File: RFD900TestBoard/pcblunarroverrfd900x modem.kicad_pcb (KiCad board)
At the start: 2 copper layers, 5.9 x 6.4 mm, 4 parts, among them J1 Barrel_Jack, J2 Conn_02x08_Counter_Clockwise, U1 ESP32-DEVKIT-V1, U2 GPS-15136

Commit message: edits
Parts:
- added R1: R, Resistor_THT:R_Axial_DIN0204_L3.6mm_D1.6mm_P1.90mm_Vertical, F.Cu at (142.8, 68.8)
- added R2: R, Resistor_THT:R_Axial_DIN0204_L3.6mm_D1.6mm_P1.90mm_Vertical, F.Cu at (177.9, 120.7)
- added R3: R, Resistor_THT:R_Axial_DIN0204_L3.6mm_D1.6mm_P1.90mm_Vertical, F.Cu at (177.9, 123.8)
- added R4: R, Resistor_THT:R_Axial_DIN0204_L3.6mm_D1.6mm_P1.90mm_Vertical, F.Cu at (177.9, 127.0)
- moved J1 63.7 mm to (206.6, 132.1), turned to 0 degrees
- moved U2 34.6 mm to (156.3, 107.1)
- moved U1 25.3 mm to (117.4, 90.7)
- moved J2 19.2 mm to (127.6, 55.9), turned to 0 degrees
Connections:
- U1 pad 11: unconnected-(U1-D21-Pad11) -> /SDA
- U1 pad 14: /CTS -> /SCL
- U1 pad 27: unconnected-(U1-D12-Pad27) -> /CTS
- U2 pad J7_1: unconnected-(U2D-SCL/SCK_J7-PadJ7_1) -> /SCL
- U2 pad J7_4: unconnected-(U2D-SDA/~{CS}_J7-PadJ7_4) -> /SDA
- U2 pad J7_7: unconnected-(U2D-3.3V_J7-PadJ7_7) -> +3.3V
- U2 pad J7_9: unconnected-(U2D-GND_J7-PadJ7_9) -> GND
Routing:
- net GND: track 137.0 -> 0.00 mm
- net +5V: track 82.1 -> 0.00 mm

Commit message: edits
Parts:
- removed R1, R2, R3, R4: R, Resistor_THT:R_Axial_DIN0204_L3.6mm_D1.6mm_P1.90mm_Vertical
- added 0.1uF1: C_Polarized_US, Capacitor_THT:CP_Radial_D5.0mm_P2.00mm, F.Cu at (169.3, 110.2)
- added 0.1uF3: C_Polarized_US, Capacitor_THT:CP_Radial_D5.0mm_P2.00mm, F.Cu at (136.7, 61.4)
- added 0.1uf2: C_Polarized_US, Capacitor_THT:CP_Radial_D5.0mm_P2.00mm, F.Cu at (104.0, 45.9)
- added 1000uf1: C_Polarized_US, Capacitor_THT:CP_Radial_D5.0mm_P2.00mm, F.Cu at (117.6, 49.4)
- added 10uF1: C_Polarized_US, Capacitor_THT:CP_Radial_D5.0mm_P2.00mm, F.Cu at (169.1, 99.8)
- added 10uF2: C_Polarized_US, Capacitor_THT:CP_Radial_D5.0mm_P2.00mm, F.Cu at (137.8, 67.0)
- added D1: LED, LED_THT:LED_D3.0mm, F.Cu at (46.0, 144.5)
- added J10: Conn_02x01, Connector_PinHeader_2.54mm:PinHeader_2x01_P2.54mm_Vertical, F.Cu at (109.8, 160.9)
- added J11: Conn_02x01, Connector_PinHeader_2.54mm:PinHeader_2x01_P2.54mm_Vertical, F.Cu at (109.8, 165.5)
- added J12: Conn_02x01, Connector_PinHeader_2.54mm:PinHeader_2x01_P2.54mm_Vertical, F.Cu at (109.8, 170.1)
- added J13: Conn_02x01, Connector_PinHeader_2.54mm:PinHeader_2x01_P2.54mm_Vertical, F.Cu at (116.9, 151.8)
- added J14: Conn_02x01, Connector_PinHeader_2.54mm:PinHeader_2x01_P2.54mm_Vertical, F.Cu at (116.9, 156.4)
- added J16: Conn_02x01, Connector_PinHeader_2.54mm:PinHeader_2x01_P2.54mm_Vertical, F.Cu at (164.2, 102.1)
- added J17: Conn_02x01, Connector_PinHeader_2.54mm:PinHeader_2x01_P2.54mm_Vertical, F.Cu at (160.4, 102.1)
- added J18: Conn_01x11, Connector_PinHeader_2.54mm:PinHeader_1x11_P2.54mm_Vertical, F.Cu at (81.8, 58.2)
- added J3: Conn_02x01, Connector_PinHeader_2.54mm:PinHeader_2x01_P2.54mm_Vertical, F.Cu at (102.6, 151.8)
- added J4: Conn_02x01, Connector_PinHeader_2.54mm:PinHeader_2x01_P2.54mm_Vertical, F.Cu at (102.6, 156.4)
- added J5: Conn_02x01, Connector_PinHeader_2.54mm:PinHeader_2x01_P2.54mm_Vertical, F.Cu at (102.6, 160.9)
- added J6: Conn_02x01, Connector_PinHeader_2.54mm:PinHeader_2x01_P2.54mm_Vertical, F.Cu at (102.6, 165.5)
- added J7: Conn_02x01, Connector_PinHeader_2.54mm:PinHeader_2x01_P2.54mm_Vertical, F.Cu at (102.6, 170.1)
- added J8: Conn_02x01, Connector_PinHeader_2.54mm:PinHeader_2x01_P2.54mm_Vertical, F.Cu at (109.8, 151.8)
- added J9: Conn_02x01, Connector_PinHeader_2.54mm:PinHeader_2x01_P2.54mm_Vertical, F.Cu at (109.8, 156.4)
- J2: footprint Connector_DIN:DIN41612_B2_2x8_Male_Horizontal_THT -> Connector_PinHeader_2.54mm:PinHeader_2x08_P2.54mm_Vertical
- moved J1 104.8 mm to (156.6, 40.0), turned to 180 degrees
- moved U2 65.1 mm to (185.3, 48.8), turned to 180 degrees
- moved J2 19.7 mm to (116.2, 39.8), turned to 90 degrees
- moved U1 8.48 mm to (118.5, 82.3)
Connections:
- U1 pad 1: +3.3V -> unconnected-(U1-3V3-Pad1)
- U1 pad 10: unconnected-(U1-D19-Pad10) -> INT
- U1 pad 11: /SDA -> SDA
- U1 pad 12: /TX -> TX-esp
- U1 pad 13: /RX -> RX-esp
- U1 pad 14: /SCL -> SCL
- U1 pad 15: /RTS -> RTS-esp
- U1 pad 23: unconnected-(U1-D25-Pad23) -> CTS-esp
- U1 pad 27: /CTS -> unconnected-(U1-D12-Pad27)
- U1 pad 4: /RESET -> unconnected-(U1-D2-Pad4)
- U1 pad 5: /SAFE -> unconnected-(U1-D4-Pad5)
- U1 pad 6: /TX2 -> TX-jet
- U1 pad 7: /RX2 -> RX-jet
- U1 pad 8: /INT -> unconnected-(U1-D5-Pad8)
- U1 pad 9: unconnected-(U1-D18-Pad9) -> RST
- U2 pad J1_2: /TX2 -> unconnected-(U2A-TX2_J1-PadJ1_2)
- U2 pad J1_3: /RX2 -> unconnected-(U2A-RX2_J1-PadJ1_3)
- U2 pad J1_4: +3.3V -> unconnected-(U2A-3.3V_J1-PadJ1_4)
- U2 pad J6_2: unconnected-(U2C-RTK_STAT-PadJ6_2) -> RTK-jet
- U2 pad J6_4: /RESET -> RST
- U2 pad J6_5: /SAFE -> unconnected-(U2C-~{SAFE}-PadJ6_5)
- U2 pad J6_6: /INT -> INT
- U2 pad J7_1: /SCL -> Net-(J12-Pin_1)
- U2 pad J7_4: /SDA -> Net-(J11-Pin_1)
- U2 pad J7_5: unconnected-(U2D-RX2_J7-PadJ7_5) -> Net-(J17-Pin_2)
- U2 pad J7_6: unconnected-(U2D-TX2_J7-PadJ7_6) -> Net-(J16-Pin_2)
- U2 pad J7_7: +3.3V -> unconnected-(U2D-3.3V_J7-PadJ7_7)
- U2 pad J7_8: unconnected-(U2D-5V_J7-PadJ7_8) -> +5V
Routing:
- net +5V: track 0.00 -> 127.6 mm
- net GND: track 0.00 -> 75.9 mm
- net TX2-jet: track 0.00 -> 17.1 mm
- net Net-(J17-Pin_2): track 0.00 -> 9.19 mm
- net Net-(J16-Pin_2): track 0.00 -> 9.07 mm
- net RX2-jet: track 0.00 -> 2.72 mm
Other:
- outline, holes or cut-outs redrawn

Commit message: changes
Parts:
- moved J10 122.7 mm to (101.5, 38.5), turned to 180 degrees
- moved J7 120.2 mm to (101.8, 50.0), turned to 180 degrees
- moved J6 120.0 mm to (135.9, 50.3), turned to 90 degrees
- moved J5 114.5 mm to (132.3, 50.3), turned to 90 degrees
- moved J9 114.5 mm to (101.8, 42.1), turned to 180 degrees
- moved J4 109.1 mm to (128.5, 50.4), turned to 90 degrees
- moved J8 106.0 mm to (101.8, 46.0), turned to 180 degrees
- moved J3 103.8 mm to (124.8, 50.4), turned to 90 degrees
- moved D1 103.0 mm to (99.5, 56.5), turned to 180 degrees
- moved J12 78.2 mm to (142.3, 99.0), turned to 180 degrees
- moved J11 68.3 mm to (142.2, 105.4), turned to 180 degrees
- moved J14 67.0 mm to (156.3, 102.1), turned to 90 degrees
- moved J13 60.9 mm to (152.2, 102.1), turned to 90 degrees
- moved 0.1uf2 47.4 mm to (150.9, 38.9), turned to -90 degrees
- moved 1000uf1 28.6 mm to (143.9, 38.2), turned to -90 degrees
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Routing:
- net RX2-jet: track 2.72 -> 140.1 mm
- net TX2-jet: track 17.1 -> 127.8 mm
- net SCL-jet: track 0.00 -> 103.1 mm
- net SDA-jet: track 0.00 -> 94.4 mm
- net INT: track 0.00 -> 92.3 mm, vias 0 -> 6
- net SDA: track 0.00 -> 88.4 mm
- net RX-esp: track 0.00 -> 80.6 mm
- net RTK-jet: track 0.00 -> 78.7 mm
- net RST: track 0.00 -> 69.1 mm, vias 0 -> 2
- net RTS-esp: track 0.00 -> 63.2 mm, vias 0 -> 2
- net TX-jet: track 0.00 -> 58.7 mm
- net TX-esp: track 0.00 -> 53.9 mm, vias 0 -> 1
- net SCL: track 0.00 -> 50.5 mm
- net RX-jet: track 0.00 -> 50.4 mm, vias 0 -> 1
- net Net-(J10-Pin_1): track 0.00 -> 41.5 mm
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- added copper zone on B.Cu, net GND

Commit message: hi
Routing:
- net GND: track 83.8 -> 68.1 mm
- net +5V: track 146.9 -> 131.8 mm
- net INT: track 92.3 -> 88.2 mm, vias 6 -> 5
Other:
- copper layers 2 -> 4
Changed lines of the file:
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@@
 	(layers
 		(0 "F.Cu" signal)
+		(4 "In1.Cu" signal)
+		(6 "In2.Cu" signal)
 		(2 "B.Cu" signal)
 		(9 "F.Adhes" user "F.Adhesive")
@@
 	)
 	(setup
+		(stackup
+			(layer "F.SilkS"
+				(type "Top Silk Screen")
+			)
+			(layer "F.Paste"
+				(type "Top Solder Paste")
+			)
+			(layer "F.Mask"
+				(type "Top Solder Mask")
+				(thickness 0.01)
+			)
+			(layer "F.Cu"
+				(type "copper")
+				(thickness 0.035)
+			)
+			(layer "dielectric 1"
+				(type "prepreg")
+				(thickness 0.1)
+				(material "FR4")
+				(epsilon_r 4.5)
+				(loss_tangent 0.02)
+			)
+			(layer "In1.Cu"
+				(type "copper")
+				(thickness 0.035)
+			)
+			(layer "dielectric 2"
+				(type "core")
+				(thickness 1.24)
+				(material "FR4")
+				(epsilon_r 4.5)
+				(loss_tangent 0.02)
+			)
+			(layer "In2.Cu"
+				(type "copper")
+				(thickness 0.035)
+			)
+			(layer "dielectric 3"
+				(type "prepreg")
+				(thickness 0.1)
+				(material "FR4")
+				(epsilon_r 4.5)
+				(loss_tangent 0.02)
+			)
+			(layer "B.Cu"
+				(type "copper")
+				(thickness 0.035)
+			)
+			(layer "B.Mask"
+				(type "Bottom Solder Mask")
+				(thickness 0.01)
+			)
+			(layer "B.Paste"
+				(type "Bottom Solder Paste")
+			)
+			(layer "B.SilkS"
+				(type "Bottom Silk Screen")
+			)
+			(copper_finish "None")
+			(dielectric_constraints no)
+		)
 		(pad_to_mask_clearance 0)
 		(allow_soldermask_bridges_in_footprints no)
@@
 	)
 	(segment
-		(start 171.674888 96.475112)
-		(end 171.674888 106.730224)
-		(width 0.7)
-		(layer "F.Cu")
-		(net 1)
-	)
-	(segment
 		(start 137.46 69.34)
 		(end 137.8 69)
@@
 	)
 	(segment
-		(start 171.32 90.72)
-		(end 171.32 96.120224)
-		(width 0.7)
-		(layer "F.Cu")
-		(net 1)
-	)
-	(segment
 		(start 165.410058 39.95)
 		(end 175.011058 49.551)
@@
 	)
 	(segment
-		(start 169.674888 96.475112)
-		(end 169.674888 91.614888)
-		(width 0.7)
-		(layer "F.Cu")
-		(net 2)
-	)
-	(segment
 		(start 123.69 33.44)
 		(end 123.55 33.3)
@@
 	)
 	(segment
-		(start 169.919776 106.975112)
-		(end 169.919776 96.72)
-		(width 0.7)
-		(layer "F.Cu")
-		(net 2)
-	)
-	(segment
 		(start 143.95 38.25)
 		(end 143.95 35.95)
@@
 	)
 	(via
-		(at 121.25 68.25)
-		(size 0.6)
-		(drill 0.3)
-		(layers "F.Cu" "B.Cu")
-		(net 48)
-	)
-	(via
 		(at 123.5 71.45)
 		(size 0.6)
@@
 	)
 	(segment
-		(start 121.3 68.25)
-		(end 121.25 68.25)
-		(width 0.2)
-		(layer "B.Cu")
-		(net 48)
-	)
-	(segment
 		(start 151.85 54.35)
 		(end 151.85 64.2)
@@
 	)
 	(segment
-		(start 103.67 87.12)
-		(end 121.3 69.49)
-		(width 0.2)
-		(layer "B.Cu")
-		(net 48)
-	)
-	(segment
 		(start 140.95 57.15)
 		(end 135.2 57.15)
@@
 	)
 	(segment
-		(start 141.1 57)
-		(end 140.95 57.15)
+		(start 109.1 85.85)
+		(end 104.94 85.85)
 		(width 0.2)
 		(layer "B.Cu")
@@
 	(segment
 		(start 123.5 71.45)
-		(end 121.25 69.2)
+		(end 109.1 85.85)
+		(width 0.2)
+		(layer "B.Cu")
+		(net 48)
+	)
+	(segment
+		(start 141.1 57)
+		(end 140.95 57.15)
 		(width 0.2)
 		(layer "B.Cu")
@@
 	)
 	(segment
-		(start 121.25 68.25)
-		(end 121.2 68.25)
-		(width 0.2)
-		(layer "B.Cu")
-		(net 48)
-	)
-	(segment
 		(start 135.2 57.15)
 		(end 135.2 59.3)
@@
 	)
 	(segment
-		(start 121.3 69.49)
-		(end 121.3 68.25)
-		(width 0.2)
-		(layer "B.Cu")
-		(net 48)
-	)
-	(segment
-		(start 121.25 69.2)
-		(end 121.25 68.25)
+		(start 104.94 85.85)
+		(end 103.67 87.12)
 		(width 0.2)
 		(layer "B.Cu")
@@
 		(min_thickness 0.25)
 		(filled_areas_thickness no)
-		(fill
+		(fill yes
 			(thermal_gap 0.5)
 			(thermal_bridge_width 0.5)

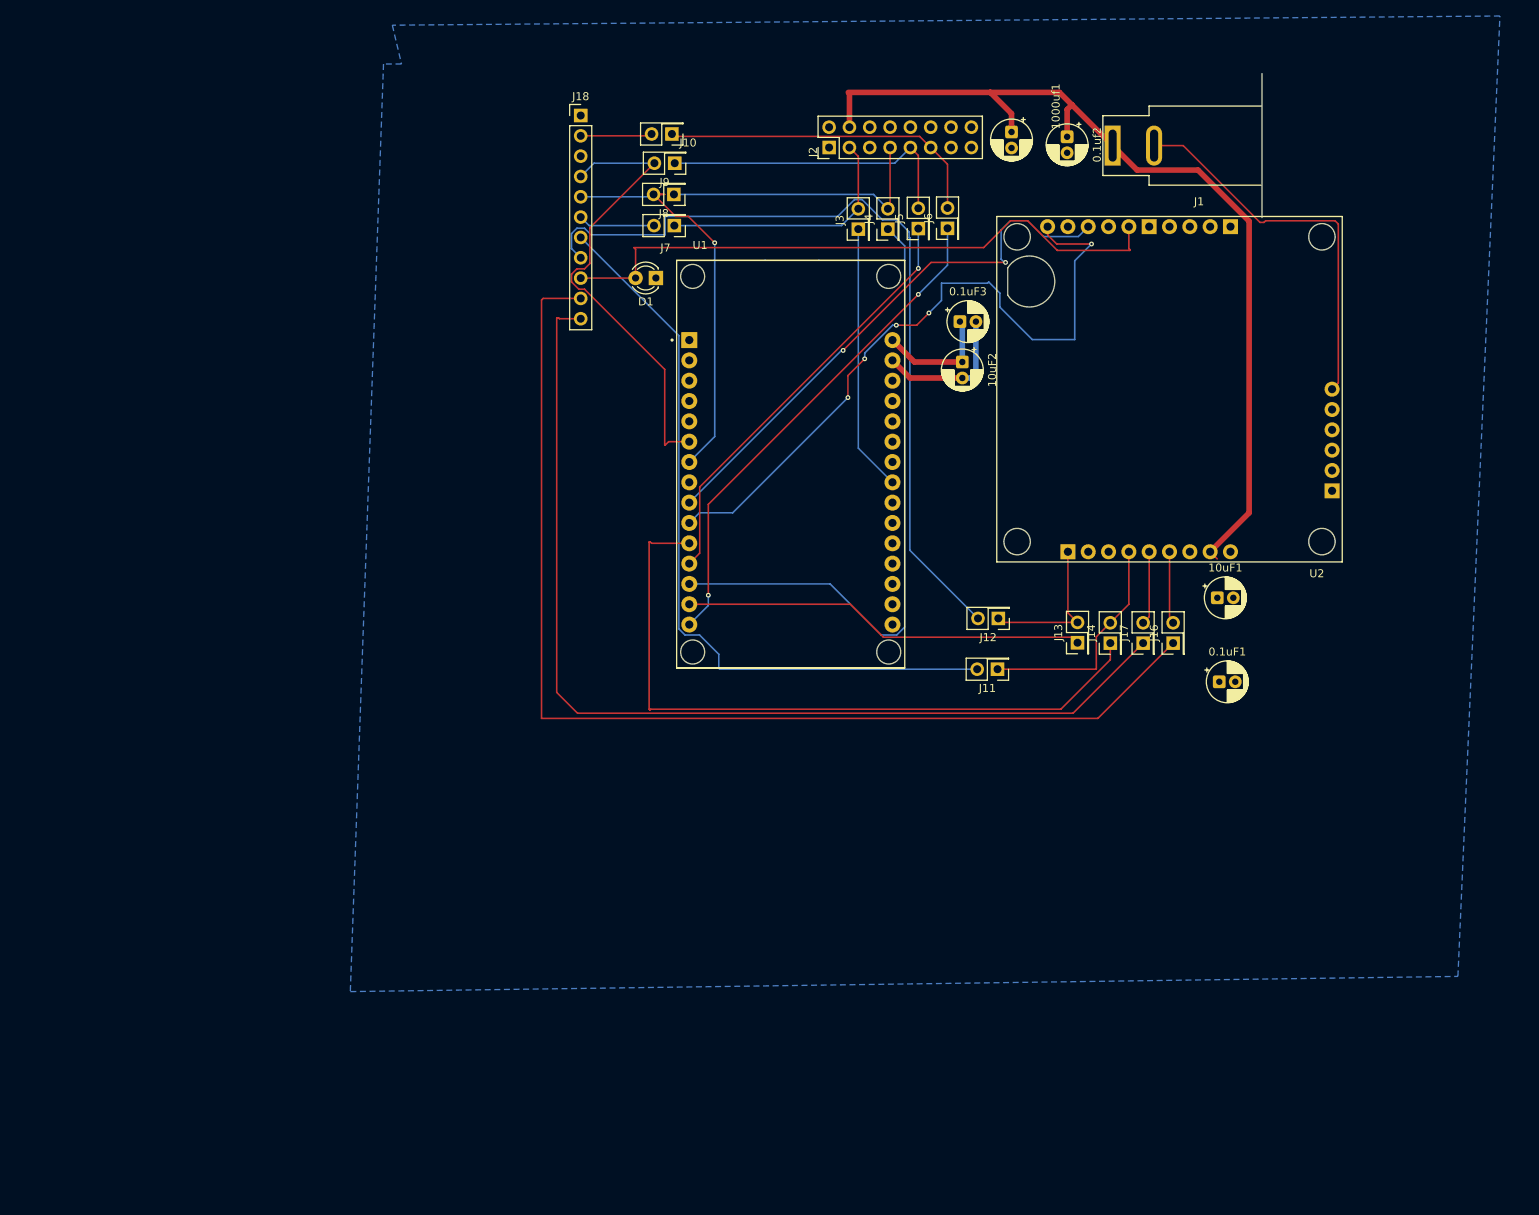
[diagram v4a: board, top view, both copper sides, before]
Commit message: made some changes to the layout of the RFD900x housing board
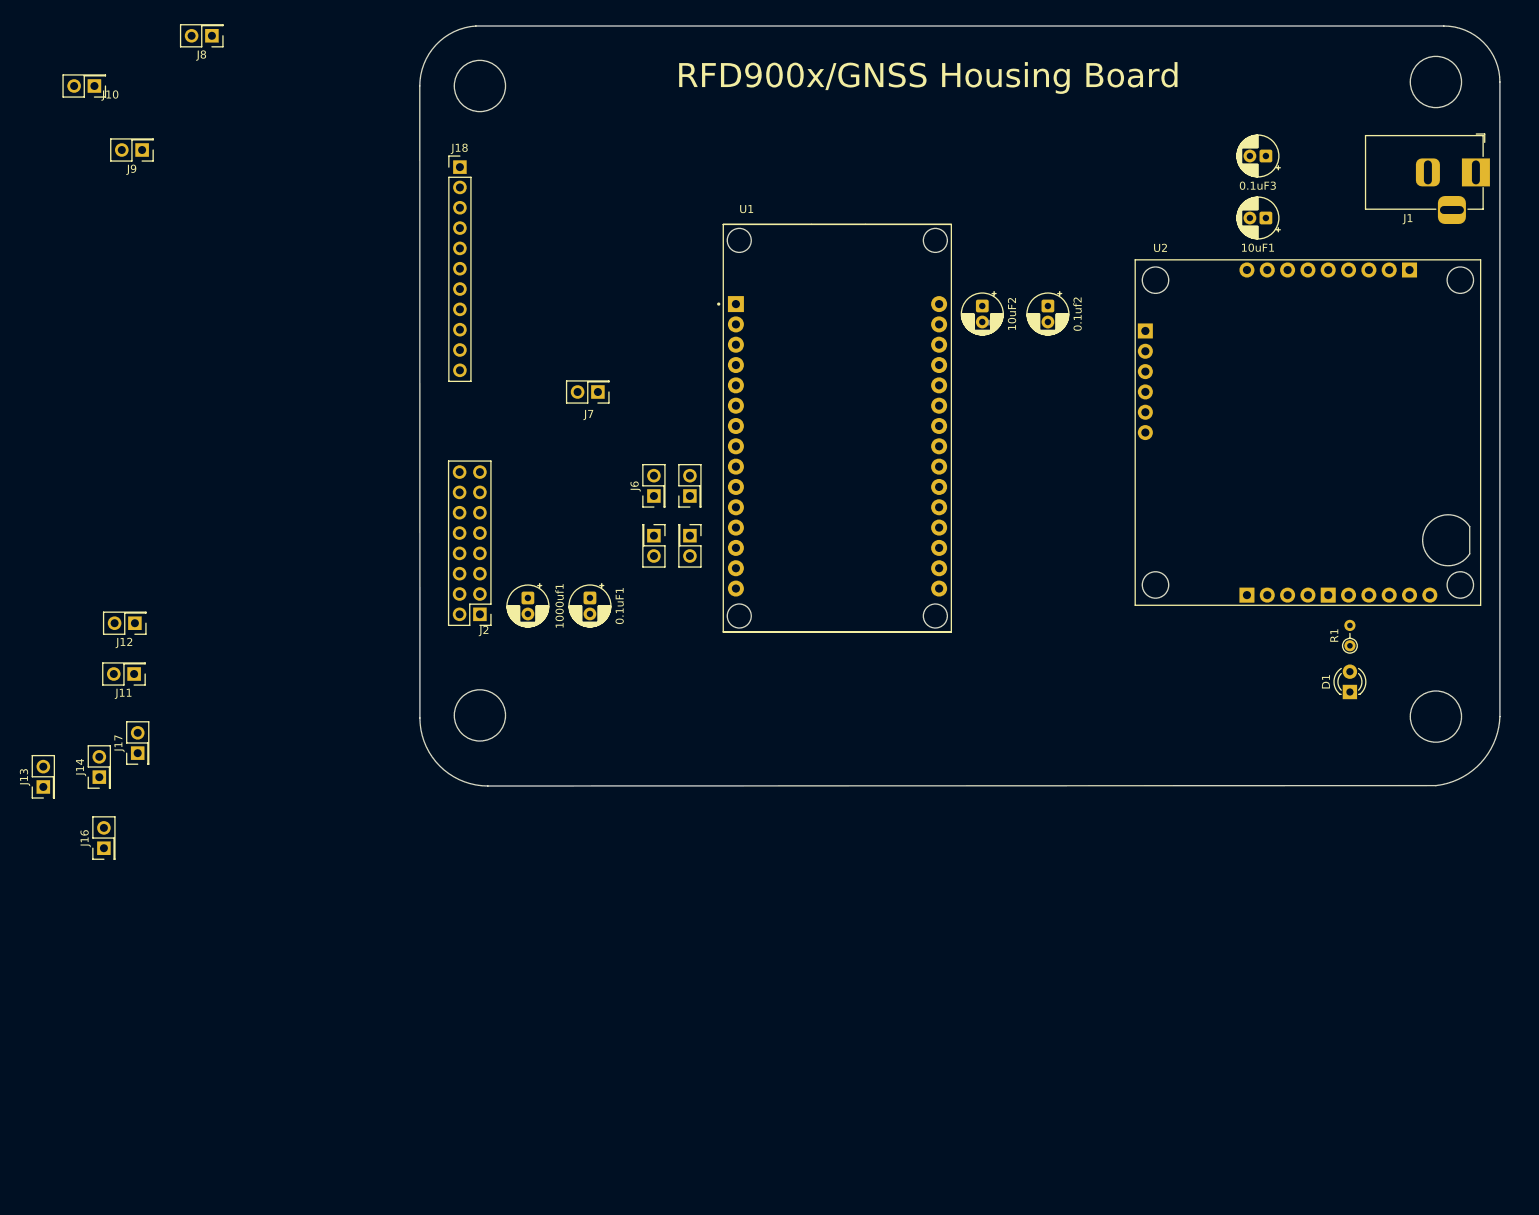
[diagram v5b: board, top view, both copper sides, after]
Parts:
- added R1: 1k, Resistor_THT:R_Axial_DIN0204_L3.6mm_D1.6mm_P2.54mm_Vertical, F.Cu at (186.2, 102.5)
- J1: value Barrel_Jack -> Barrel_Jack_Switch; footprint Connector_BarrelJack:BarrelJack_SwitchcraftConxall_RAPC10U_Horizontal -> Connector_BarrelJack:BarrelJack_Horizontal
- moved J16 136.1 mm to (30.5, 127.8)
- moved J13 130.5 mm to (22.9, 120.1)
- moved J14 127.5 mm to (29.9, 118.9)
- moved J17 126.4 mm to (34.7, 115.9)
- moved J12 107.9 mm to (34.4, 99.7)
- moved J11 107.9 mm to (34.3, 106.0)
- moved D1 101.0 mm to (186.2, 108.2), turned to 90 degrees
- moved 1000uf1 83.9 mm to (83.5, 96.5)
- moved 0.1uF1 79.4 mm to (91.3, 96.5), turned to -90 degrees
- moved J2 72.9 mm to (77.5, 98.5), turned to 180 degrees
- moved J10 72.4 mm to (29.3, 32.5)
- moved J9 66.6 mm to (35.3, 40.5)
- moved J8 61.1 mm to (44.0, 26.2)
- moved U2 55.1 mm to (159.4, 97.4), turned to 0 degrees
- moved J6 49.7 mm to (99.2, 83.8)
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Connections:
- D1 pad 2: RTK-jet -> Net-(D1-A)
- J10 pad 1: Net-(J10-Pin_1) -> RTS
- J2 pad 1: GND -> unconnected-(J2-Pin_1-Pad1)
- J2 pad 10: unconnected-(J2-Pin_10-Pad10) -> TX
- J2 pad 11: Net-(J10-Pin_1) -> unconnected-(J2-Pin_11-Pad11)
- J2 pad 12: unconnected-(J2-Pin_12-Pad12) -> RTS
- J2 pad 2: unconnected-(J2-Pin_2-Pad2) -> GND
- J2 pad 3: Net-(J2-Pin_3) -> +5V
- J2 pad 4: +5V -> CTS
- J2 pad 7: Net-(J2-Pin_7) -> unconnected-(J2-Pin_7-Pad7)
- J2 pad 8: unconnected-(J2-Pin_8-Pad8) -> RX
- J2 pad 9: Net-(J2-Pin_9) -> unconnected-(J2-Pin_9-Pad9)
- J3 pad 2: Net-(J2-Pin_3) -> CTS
- J4 pad 2: Net-(J2-Pin_7) -> RX
- J5 pad 2: Net-(J2-Pin_9) -> TX
- J6 pad 2: Net-(J10-Pin_1) -> RTS
- J7 pad 1: Net-(J2-Pin_3) -> CTS
- J8 pad 1: Net-(J2-Pin_7) -> RX
- J9 pad 1: Net-(J2-Pin_9) -> TX
- U1 pad 12: TX-esp -> RX-esp
- U1 pad 13: RX-esp -> TX-esp
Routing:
- net RX2-jet: track 140.1 -> 0.00 mm
- net +5V: track 131.8 -> 0.77 mm
- net TX2-jet: track 127.8 -> 0.00 mm
- net SCL-jet: track 103.1 -> 0.00 mm
- net SDA-jet: track 94.4 -> 0.00 mm
- net SDA: track 88.4 -> 0.00 mm
- net INT: track 88.2 -> 0.00 mm, vias 5 -> 0
- net RX-esp: track 80.6 -> 0.00 mm
- net RTK-jet: track 78.7 -> 0.00 mm
- net RST: track 69.1 -> 0.00 mm, vias 2 -> 0
- net GND: track 68.1 -> 2.76 mm
- net RTS-esp: track 63.2 -> 0.00 mm, vias 2 -> 0
- net TX-jet: track 58.7 -> 0.00 mm
- net TX-esp: track 53.9 -> 0.00 mm, vias 1 -> 0
- net SCL: track 50.5 -> 0.00 mm
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- added copper zone on In1.Cu, net GND
- removed copper zone on B.Cu, net GND
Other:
- board size 5.9 x 6.4 mm -> 135 x 95 mm
- board text added: "RFD900x/GNSS Housing Board"
